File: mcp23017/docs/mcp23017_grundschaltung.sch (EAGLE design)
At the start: 2 parts, among them IC1 MCP23017SP

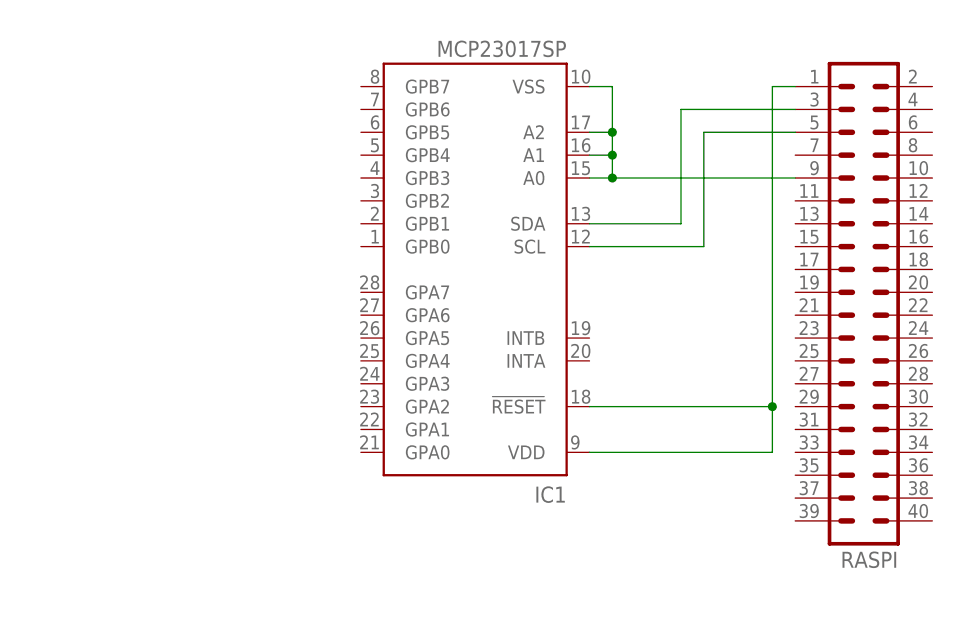
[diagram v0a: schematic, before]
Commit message: reorganization circuit
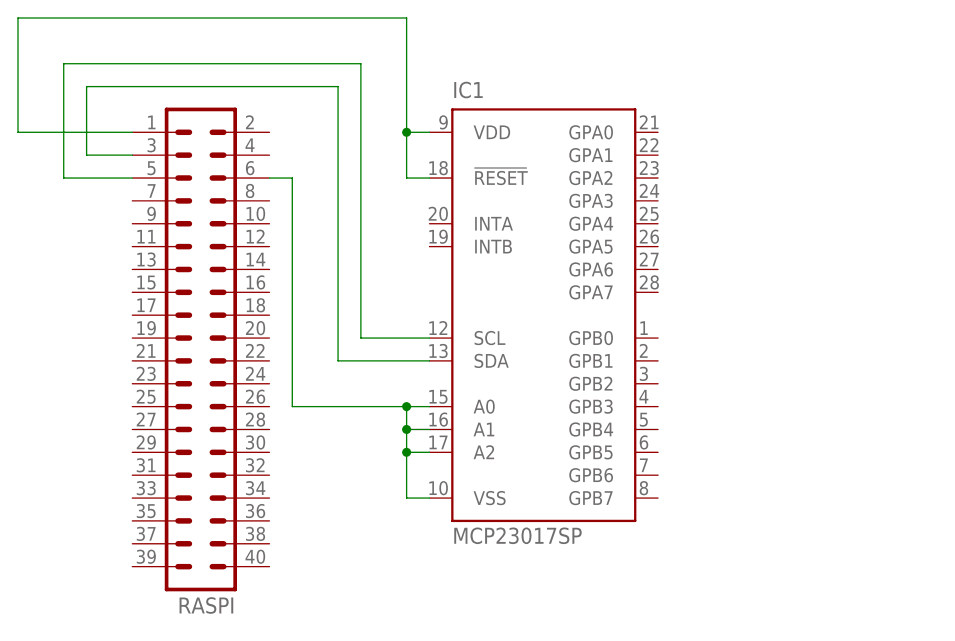
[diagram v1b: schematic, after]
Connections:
- net N$2: now also RASPI.6; no longer RASPI.9
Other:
- moved on the sheet: IC1, RASPI
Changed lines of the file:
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@@
 </plain>
 <instances>
-<instance part="IC1" gate="G$1" x="66.04" y="45.72" rot="R180"/>
-<instance part="RASPI" gate="1" x="109.22" y="40.64" rot="R180"/>
+<instance part="IC1" gate="G$1" x="73.66" y="40.64"/>
+<instance part="RASPI" gate="1" x="35.56" y="35.56" rot="R180"/>
 </instances>
 <busses>
 </busses>
 <nets>
-<net name="N$1" class="0">
+<net name="N$3" class="0">
 <segment>
-<pinref part="RASPI" gate="1" pin="1"/>
-<wire x1="101.6" y1="66.04" x2="99.06" y2="66.04" width="0.1524" layer="91"/>
-<wire x1="99.06" y1="66.04" x2="99.06" y2="30.48" width="0.1524" layer="91"/>
-<pinref part="IC1" gate="G$1" pin="VDD"/>
-<wire x1="99.06" y1="30.48" x2="99.06" y2="25.4" width="0.1524" layer="91"/>
-<wire x1="99.06" y1="25.4" x2="78.74" y2="25.4" width="0.1524" layer="91"/>
-<pinref part="IC1" gate="G$1" pin="!RESET"/>
-<wire x1="78.74" y1="30.48" x2="99.06" y2="30.48" width="0.1524" layer="91"/>
-<junction x="99.06" y="30.48"/>
+<wire x1="22.86" y1="66.04" x2="22.86" y2="58.42" width="0.1524" layer="91"/>
+<pinref part="RASPI" gate="1" pin="3"/>
+<wire x1="22.86" y1="58.42" x2="27.94" y2="58.42" width="0.1524" layer="91"/>
+<wire x1="22.86" y1="66.04" x2="50.8" y2="66.04" width="0.1524" layer="91"/>
+<wire x1="50.8" y1="66.04" x2="50.8" y2="35.56" width="0.1524" layer="91"/>
+<pinref part="IC1" gate="G$1" pin="SDA"/>
+<wire x1="50.8" y1="35.56" x2="60.96" y2="35.56" width="0.1524" layer="91"/>
+</segment>
+</net>
+<net name="N$4" class="0">
+<segment>
+<wire x1="20.32" y1="68.58" x2="20.32" y2="55.88" width="0.1524" layer="91"/>
+<pinref part="RASPI" gate="1" pin="5"/>
+<wire x1="20.32" y1="55.88" x2="27.94" y2="55.88" width="0.1524" layer="91"/>
+<wire x1="20.32" y1="68.58" x2="53.34" y2="68.58" width="0.1524" layer="91"/>
+<wire x1="53.34" y1="68.58" x2="53.34" y2="38.1" width="0.1524" layer="91"/>
+<pinref part="IC1" gate="G$1" pin="SCL"/>
+<wire x1="53.34" y1="38.1" x2="60.96" y2="38.1" width="0.1524" layer="91"/>
 </segment>
 </net>
@@
 <segment>
 <pinref part="IC1" gate="G$1" pin="VSS"/>
-<wire x1="78.74" y1="66.04" x2="81.28" y2="66.04" width="0.1524" layer="91"/>
-<wire x1="81.28" y1="66.04" x2="81.28" y2="60.96" width="0.1524" layer="91"/>
-<pinref part="RASPI" gate="1" pin="9"/>
-<wire x1="81.28" y1="60.96" x2="81.28" y2="58.42" width="0.1524" layer="91"/>
-<wire x1="81.28" y1="58.42" x2="81.28" y2="55.88" width="0.1524" layer="91"/>
-<wire x1="81.28" y1="55.88" x2="101.6" y2="55.88" width="0.1524" layer="91"/>
+<wire x1="60.96" y1="20.32" x2="58.42" y2="20.32" width="0.1524" layer="91"/>
+<pinref part="RASPI" gate="1" pin="6"/>
+<wire x1="43.18" y1="55.88" x2="45.72" y2="55.88" width="0.1524" layer="91"/>
+<wire x1="45.72" y1="55.88" x2="45.72" y2="30.48" width="0.1524" layer="91"/>
 <pinref part="IC1" gate="G$1" pin="A0"/>
-<wire x1="78.74" y1="55.88" x2="81.28" y2="55.88" width="0.1524" layer="91"/>
-<junction x="81.28" y="55.88"/>
+<wire x1="60.96" y1="30.48" x2="58.42" y2="30.48" width="0.1524" layer="91"/>
+<wire x1="58.42" y1="30.48" x2="58.42" y2="27.94" width="0.1524" layer="91"/>
 <pinref part="IC1" gate="G$1" pin="A1"/>
-<wire x1="78.74" y1="58.42" x2="81.28" y2="58.42" width="0.1524" layer="91"/>
-<junction x="81.28" y="58.42"/>
+<wire x1="58.42" y1="27.94" x2="58.42" y2="25.4" width="0.1524" layer="91"/>
+<wire x1="58.42" y1="25.4" x2="58.42" y2="20.32" width="0.1524" layer="91"/>
+<wire x1="60.96" y1="27.94" x2="58.42" y2="27.94" width="0.1524" layer="91"/>
+<junction x="58.42" y="27.94"/>
 <pinref part="IC1" gate="G$1" pin="A2"/>
-<wire x1="78.74" y1="60.96" x2="81.28" y2="60.96" width="0.1524" layer="91"/>
-<junction x="81.28" y="60.96"/>
+<wire x1="60.96" y1="25.4" x2="58.42" y2="25.4" width="0.1524" layer="91"/>
+<junction x="58.42" y="25.4"/>
+<wire x1="58.42" y1="30.48" x2="45.72" y2="30.48" width="0.1524" layer="91"/>
+<junction x="58.42" y="30.48"/>
 </segment>
 </net>
-<net name="N$3" class="0">
+<net name="N$5" class="0">
 <segment>
-<pinref part="IC1" gate="G$1" pin="SDA"/>
-<wire x1="78.74" y1="50.8" x2="88.9" y2="50.8" width="0.1524" layer="91"/>
-<wire x1="88.9" y1="50.8" x2="88.9" y2="63.5" width="0.1524" layer="91"/>
-<pinref part="RASPI" gate="1" pin="3"/>
-<wire x1="88.9" y1="63.5" x2="101.6" y2="63.5" width="0.1524" layer="91"/>
+<pinref part="RASPI" gate="1" pin="1"/>
+<wire x1="27.94" y1="60.96" x2="15.24" y2="60.96" width="0.1524" layer="91"/>
+<wire x1="15.24" y1="60.96" x2="15.24" y2="73.66" width="0.1524" layer="91"/>
+<wire x1="15.24" y1="73.66" x2="58.42" y2="73.66" width="0.1524" layer="91"/>
+<wire x1="58.42" y1="73.66" x2="58.42" y2="60.96" width="0.1524" layer="91"/>
+<pinref part="IC1" gate="G$1" pin="VDD"/>
+<wire x1="58.42" y1="60.96" x2="60.96" y2="60.96" width="0.1524" layer="91"/>
+<pinref part="IC1" gate="G$1" pin="!RESET"/>
+<wire x1="60.96" y1="55.88" x2="58.42" y2="55.88" width="0.1524" layer="91"/>
+<wire x1="58.42" y1="55.88" x2="58.42" y2="60.96" width="0.1524" layer="91"/>
+<junction x="58.42" y="60.96"/>
 </segment>
 </net>
-<net name="N$4" class="0">
-<segment>
-<pinref part="IC1" gate="G$1" pin="SCL"/>
-<wire x1="78.74" y1="48.26" x2="91.44" y2="48.26" width="0.1524" layer="91"/>
-<wire x1="91.44" y1="48.26" x2="91.44" y2="60.96" width="0.1524" layer="91"/>
-<pinref part="RASPI" gate="1" pin="5"/>
-<wire x1="91.44" y1="60.96" x2="101.6" y2="60.96" width="0.1524" layer="91"/>
-</segment>
-</net>
